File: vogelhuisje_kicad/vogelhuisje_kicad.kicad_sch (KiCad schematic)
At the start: 1 part, among them J6 Conn_01x19_Female

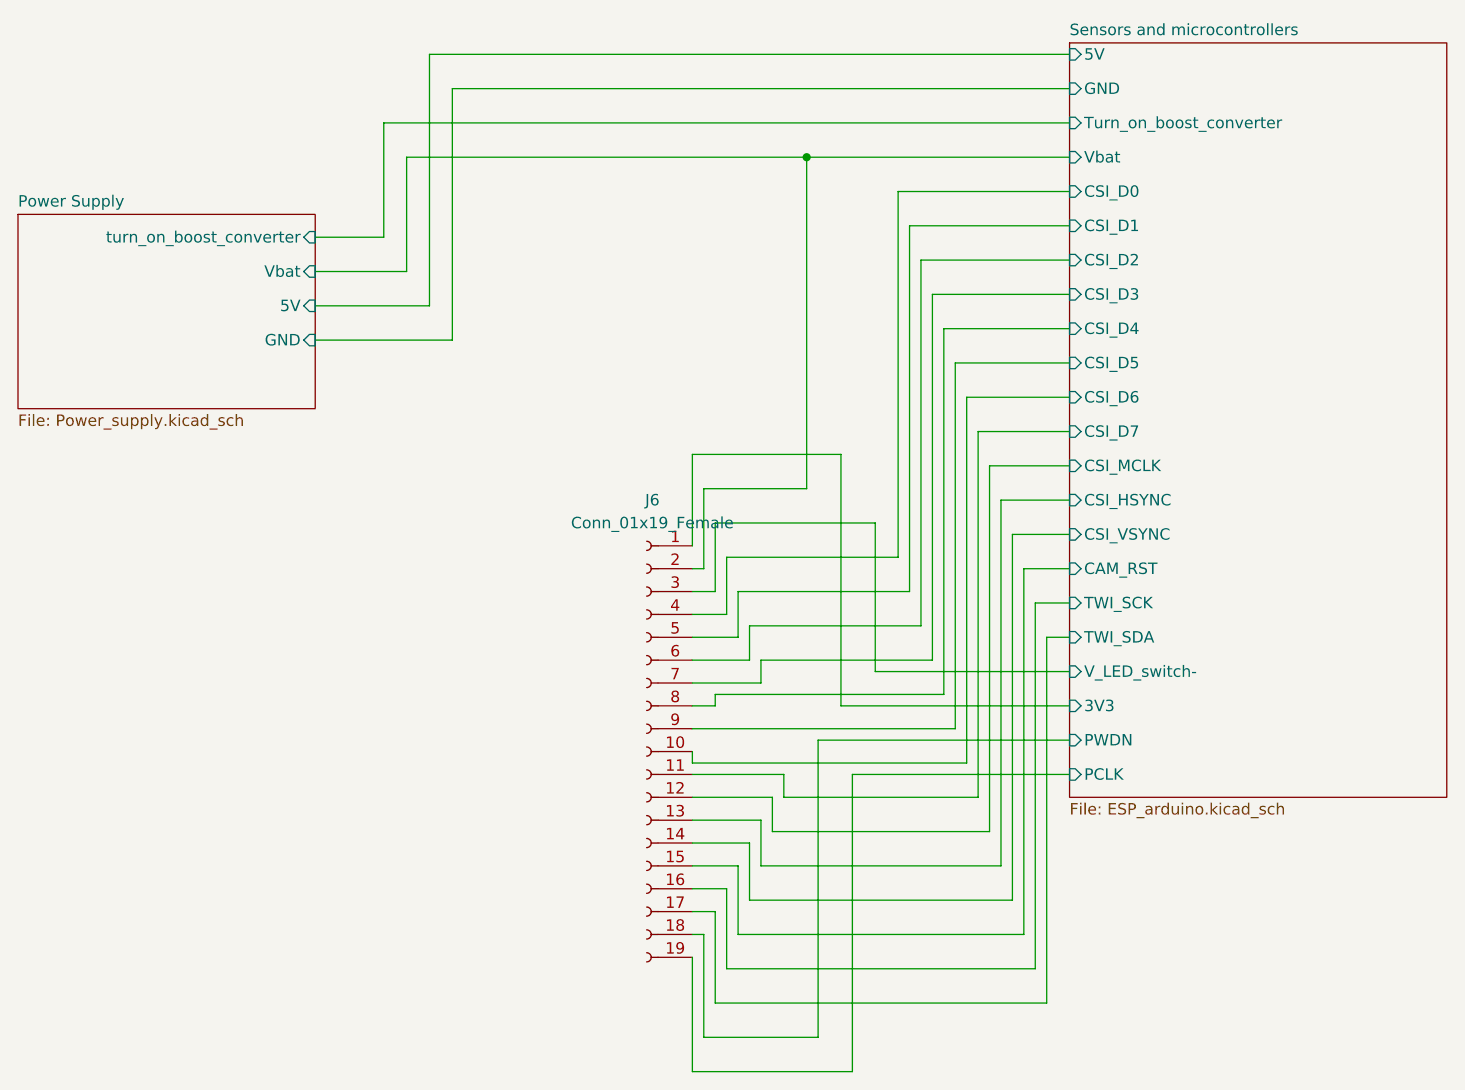
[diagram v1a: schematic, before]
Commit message: Kicad Changes Tadjiro
Board now supports 3 lipo cells and a motion sensor.
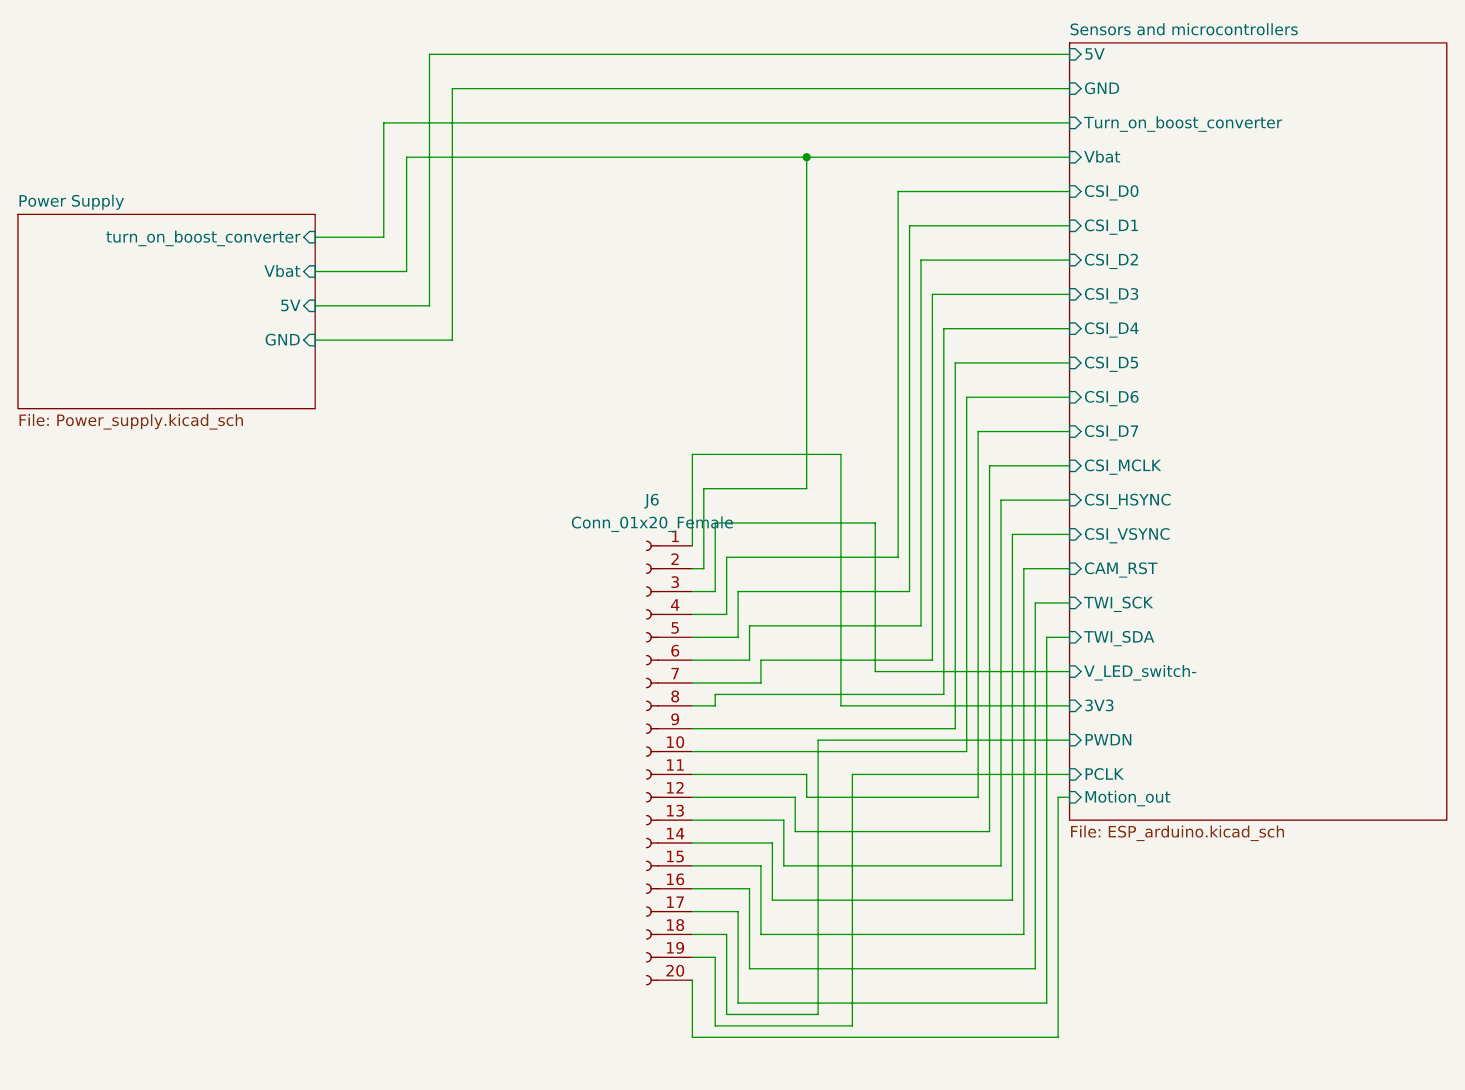
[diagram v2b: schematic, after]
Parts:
- J6: value Conn_01x19_Female -> Conn_01x20_Female; footprint Connector_PinHeader_2.54mm:PinHeader_1x19_P2.54mm_Vertical -> Connector_PinHeader_2.54mm:PinHeader_1x20_P2.54mm_Vertical; symbol Connector:Conn_01x19_Female -> Connector:Conn_01x20_Female
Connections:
- new net Sensors and microcontrollers/Motion_out: J6.20 (Pin_20)
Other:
- sheet Sensors and microcontrollers ports: added Motion_out; removed none

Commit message: Update main board
Ground port added to connector
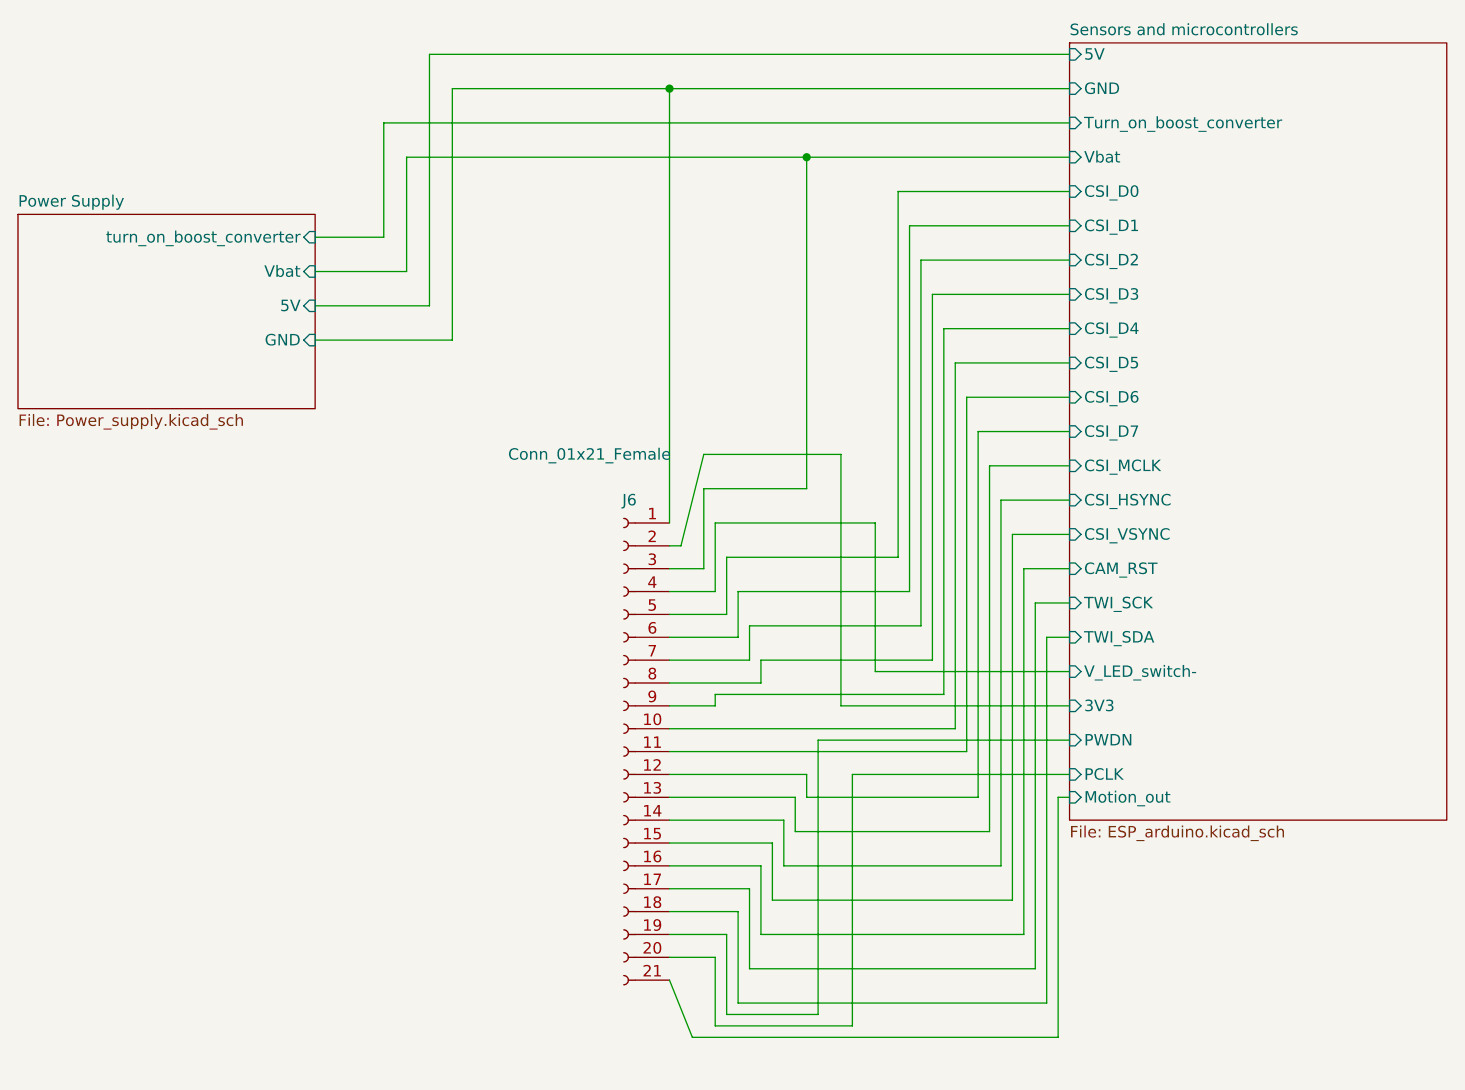
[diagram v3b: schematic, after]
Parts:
- J6: value Conn_01x20_Female -> Conn_01x21_Female; footprint Connector_PinHeader_2.54mm:PinHeader_1x20_P2.54mm_Vertical -> Connector_PinHeader_2.54mm:PinHeader_1x21_P2.54mm_Vertical; symbol Connector:Conn_01x20_Female -> Connector:Conn_01x21_Female
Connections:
- net Power Supply/GND: now also J6.1 (Pin_1)
- net Power Supply/Vbat: now also J6.3 (Pin_3); no longer J6.2 (Pin_2)
- net Sensors and microcontrollers/3V3: now also J6.2 (Pin_2); no longer J6.1 (Pin_1)
- net Sensors and microcontrollers/CAM_RST: now also J6.16 (Pin_16); no longer J6.15 (Pin_15)
- net Sensors and microcontrollers/CSI_D0: now also J6.5 (Pin_5); no longer J6.4 (Pin_4)
- net Sensors and microcontrollers/CSI_D1: now also J6.6 (Pin_6); no longer J6.5 (Pin_5)
- net Sensors and microcontrollers/CSI_D2: now also J6.7 (Pin_7); no longer J6.6 (Pin_6)
- net Sensors and microcontrollers/CSI_D3: now also J6.8 (Pin_8); no longer J6.7 (Pin_7)
- net Sensors and microcontrollers/CSI_D4: now also J6.9 (Pin_9); no longer J6.8 (Pin_8)
- net Sensors and microcontrollers/CSI_D5: now also J6.10 (Pin_10); no longer J6.9 (Pin_9)
- net Sensors and microcontrollers/CSI_D6: now also J6.11 (Pin_11); no longer J6.10 (Pin_10)
- net Sensors and microcontrollers/CSI_D7: now also J6.12 (Pin_12); no longer J6.11 (Pin_11)
- net Sensors and microcontrollers/CSI_HSYNC: now also J6.14 (Pin_14); no longer J6.13 (Pin_13)
- net Sensors and microcontrollers/CSI_MCLK: now also J6.13 (Pin_13); no longer J6.12 (Pin_12)
- net Sensors and microcontrollers/CSI_VSYNC: now also J6.15 (Pin_15); no longer J6.14 (Pin_14)
- net Sensors and microcontrollers/Motion_out: now also J6.21 (Pin_21); no longer J6.20 (Pin_20)
- net Sensors and microcontrollers/PCLK: now also J6.20 (Pin_20); no longer J6.19 (Pin_19)
- net Sensors and microcontrollers/PWDN: now also J6.19 (Pin_19); no longer J6.18 (Pin_18)
- net Sensors and microcontrollers/TWI_SCK: now also J6.17 (Pin_17); no longer J6.16 (Pin_16)
- net Sensors and microcontrollers/TWI_SDA: now also J6.18 (Pin_18); no longer J6.17 (Pin_17)
- net Sensors and microcontrollers/V_LED_switch-: now also J6.4 (Pin_4); no longer J6.3 (Pin_3)
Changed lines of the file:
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@@
 (kicad_sch (version 20211123) (generator eeschema)
   (paper "A4")
+  (junction (at 115.57 44.45) (diameter 0) (color 0 0 0 0)
+  )
   (junction (at 130.81 52.07) (diameter 0) (color 0 0 0 0)
   )
@@
     (stroke (width 0) (type default) (color 0 0 0 0))
   )
-  (wire (pts (xy 125.73 130.81) (xy 118.11 130.81))
+  (wire (pts (xy 125.73 130.81) (xy 115.57 130.81))
     (stroke (width 0) (type default) (color 0 0 0 0))
   )
@@
     (stroke (width 0) (type default) (color 0 0 0 0))
   )
-  (wire (pts (xy 125.73 110.49) (xy 118.11 110.49))
+  (wire (pts (xy 125.73 110.49) (xy 115.57 110.49))
     (stroke (width 0) (type default) (color 0 0 0 0))
   )
@@
     (stroke (width 0) (type default) (color 0 0 0 0))
   )
+  (wire (pts (xy 116.84 95.25) (xy 115.57 95.25))
+    (stroke (width 0) (type default) (color 0 0 0 0))
+  )
   (wire (pts (xy 144.78 67.31) (xy 160.02 67.31))
     (stroke (width 0) (type default) (color 0 0 0 0))
   )
-  (wire (pts (xy 124.46 107.95) (xy 118.11 107.95))
+  (wire (pts (xy 124.46 107.95) (xy 115.57 107.95))
     (stroke (width 0) (type default) (color 0 0 0 0))
   )
@@
     (stroke (width 0) (type default) (color 0 0 0 0))
   )
-  (wire (pts (xy 91.44 44.45) (xy 160.02 44.45))
+  (wire (pts (xy 91.44 44.45) (xy 115.57 44.45))
     (stroke (width 0) (type default) (color 0 0 0 0))
   )
@@
     (stroke (width 0) (type default) (color 0 0 0 0))
   )
-  (wire (pts (xy 118.11 118.11) (xy 148.59 118.11))
+  (wire (pts (xy 115.57 118.11) (xy 148.59 118.11))
     (stroke (width 0) (type default) (color 0 0 0 0))
   )
@@
     (stroke (width 0) (type default) (color 0 0 0 0))
   )
-  (wire (pts (xy 129.54 123.19) (xy 118.11 123.19))
-    (stroke (width 0) (type default) (color 0 0 0 0))
-  )
-  (wire (pts (xy 118.11 143.51) (xy 118.11 149.86))
-    (stroke (width 0) (type default) (color 0 0 0 0))
-  )
-  (wire (pts (xy 121.92 102.87) (xy 118.11 102.87))
+  (wire (pts (xy 129.54 123.19) (xy 115.57 123.19))
+    (stroke (width 0) (type default) (color 0 0 0 0))
+  )
+  (wire (pts (xy 115.57 143.51) (xy 118.11 149.86))
+    (stroke (width 0) (type default) (color 0 0 0 0))
+  )
+  (wire (pts (xy 115.57 44.45) (xy 115.57 92.71))
+    (stroke (width 0) (type default) (color 0 0 0 0))
+  )
+  (wire (pts (xy 121.92 102.87) (xy 115.57 102.87))
     (stroke (width 0) (type default) (color 0 0 0 0))
   )
@@
     (stroke (width 0) (type default) (color 0 0 0 0))
   )
-  (wire (pts (xy 119.38 97.79) (xy 118.11 97.79))
+  (wire (pts (xy 119.38 97.79) (xy 115.57 97.79))
     (stroke (width 0) (type default) (color 0 0 0 0))
   )
@@
     (stroke (width 0) (type default) (color 0 0 0 0))
   )
-  (wire (pts (xy 127 128.27) (xy 118.11 128.27))
+  (wire (pts (xy 127 128.27) (xy 115.57 128.27))
     (stroke (width 0) (type default) (color 0 0 0 0))
   )
@@
     (stroke (width 0) (type default) (color 0 0 0 0))
   )
-  (wire (pts (xy 121.92 138.43) (xy 118.11 138.43))
-    (stroke (width 0) (type default) (color 0 0 0 0))
-  )
-  (wire (pts (xy 118.11 115.57) (xy 147.32 115.57))
-    (stroke (width 0) (type default) (color 0 0 0 0))
-  )
-  (wire (pts (xy 120.65 100.33) (xy 118.11 100.33))
-    (stroke (width 0) (type default) (color 0 0 0 0))
-  )
-  (wire (pts (xy 118.11 85.09) (xy 118.11 95.25))
-    (stroke (width 0) (type default) (color 0 0 0 0))
-  )
-  (wire (pts (xy 123.19 105.41) (xy 118.11 105.41))
+  (wire (pts (xy 121.92 138.43) (xy 115.57 138.43))
+    (stroke (width 0) (type default) (color 0 0 0 0))
+  )
+  (wire (pts (xy 115.57 44.45) (xy 160.02 44.45))
+    (stroke (width 0) (type default) (color 0 0 0 0))
+  )
+  (wire (pts (xy 115.57 115.57) (xy 147.32 115.57))
+    (stroke (width 0) (type default) (color 0 0 0 0))
+  )
+  (wire (pts (xy 120.65 100.33) (xy 115.57 100.33))
+    (stroke (width 0) (type default) (color 0 0 0 0))
+  )
+  (wire (pts (xy 119.38 85.09) (xy 116.84 95.25))
+    (stroke (width 0) (type default) (color 0 0 0 0))
+  )
+  (wire (pts (xy 123.19 105.41) (xy 115.57 105.41))
     (stroke (width 0) (type default) (color 0 0 0 0))
   )
@@
     (stroke (width 0) (type default) (color 0 0 0 0))
   )
-  (wire (pts (xy 120.65 113.03) (xy 118.11 113.03))
+  (wire (pts (xy 120.65 113.03) (xy 115.57 113.03))
     (stroke (width 0) (type default) (color 0 0 0 0))
   )
@@
     (stroke (width 0) (type default) (color 0 0 0 0))
   )
-  (wire (pts (xy 118.11 120.65) (xy 130.81 120.65))
+  (wire (pts (xy 115.57 120.65) (xy 130.81 120.65))
     (stroke (width 0) (type default) (color 0 0 0 0))
   )
@@
     (stroke (width 0) (type default) (color 0 0 0 0))
   )
-  (wire (pts (xy 120.65 140.97) (xy 118.11 140.97))
-    (stroke (width 0) (type default) (color 0 0 0 0))
-  )
-  (wire (pts (xy 124.46 133.35) (xy 118.11 133.35))
+  (wire (pts (xy 120.65 140.97) (xy 115.57 140.97))
+    (stroke (width 0) (type default) (color 0 0 0 0))
+  )
+  (wire (pts (xy 124.46 133.35) (xy 115.57 133.35))
     (stroke (width 0) (type default) (color 0 0 0 0))
   )
@@
     (stroke (width 0) (type default) (color 0 0 0 0))
   )
-  (wire (pts (xy 128.27 125.73) (xy 118.11 125.73))
-    (stroke (width 0) (type default) (color 0 0 0 0))
-  )
-  (wire (pts (xy 123.19 135.89) (xy 118.11 135.89))
+  (wire (pts (xy 128.27 125.73) (xy 115.57 125.73))
+    (stroke (width 0) (type default) (color 0 0 0 0))
+  )
+  (wire (pts (xy 123.19 135.89) (xy 115.57 135.89))
     (stroke (width 0) (type default) (color 0 0 0 0))
   )
@@
     (stroke (width 0) (type default) (color 0 0 0 0))
   )
-  (wire (pts (xy 118.11 85.09) (xy 134.62 85.09))
+  (wire (pts (xy 119.38 85.09) (xy 134.62 85.09))
     (stroke (width 0) (type default) (color 0 0 0 0))
   )
@@
     (stroke (width 0) (type default) (color 0 0 0 0))
   )
-  (symbol (lib_id "Connector:Conn_01x20_Female") (at 113.03 118.11 0) (mirror y) (unit 1)
-    (in_bom yes) (on_board yes) (fields_autoplaced)
-    (property "Reference" "J6" (id 0) (at 113.665 90.17 0))
-    (property "Value" "Conn_01x20_Female" (id 1) (at 113.665 92.71 0))
-    (property "Footprint" "Connector_PinHeader_2.54mm:PinHeader_1x20_P2.54mm_Vertical" (id 2) (at 113.03 118.11 0)
+  (symbol (lib_id "Connector:Conn_01x21_Female") (at 110.49 118.11 0) (mirror y) (unit 1)
+    (in_bom yes) (on_board yes)
+    (property "Reference" "J6" (id 0) (at 111.125 90.17 0))
+    (property "Value" "Conn_01x21_Female" (id 1) (at 106.68 85.09 0))
+    (property "Footprint" "Connector_PinHeader_2.54mm:PinHeader_1x21_P2.54mm_Vertical" (id 2) (at 110.49 118.11 0)
       (effects (font (size 1.27 1.27)) hide)
     )
-    (property "Datasheet" "~" (id 3) (at 113.03 118.11 0)
+    (property "Datasheet" "~" (id 3) (at 110.49 118.11 0)
       (effects (font (size 1.27 1.27)) hide)
     )
@@
     (pin "2")
     (pin "20")
+    (pin "21")
     (pin "3")
     (pin "4")
@@
     )
     (path "/0e668d66-c2e4-40fb-b10d-c3f215200616"
-      (reference "J6") (unit 1) (value "Conn_01x20_Female") (footprint "Connector_PinHeader_2.54mm:PinHeader_1x20_P2.54mm_Vertical")
+      (reference "J6") (unit 1) (value "Conn_01x21_Female") (footprint "Connector_PinHeader_2.54mm:PinHeader_1x21_P2.54mm_Vertical")
     )
     (path "/00000000-0000-0000-0000-00006263b8ad/e30e354a-54cb-4067-a3a3-e7d7fc5351da"
